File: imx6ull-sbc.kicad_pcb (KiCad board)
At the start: 4 copper layers, 210 parts, among them J1 Micro_SD_Card_Det1, J2 USB4105, J3 USB1130, J4 USB4105, J5 Barrel_Jack_Switch, J6 CRJ011-ML3-TH, Q1 SiSA35DN, SW1 CAS-220TA, U1 MX6UL-VM, U10 SFEM064GB1ED1TO-I-6F-111-STD, U11 TPD4EUSB30, U12 74LVC1G06, U13 D5V0H1B2LP, U14 D5V0H1B2LP, U15 TPS54233, U16 TPS2116DRLR, U17 INA219BxD, U18 DP83825IRMQR, U2 MC32PF1510A6EP, U3 MT41K256M16, U4 TUSB320, U5 AP22814AW5, U6 TPD4EUSB30, U7 D5V0H1B2LP, U8 D5V0H1B2LP, U9 W25Q32JVZP, Y1 24Mhz, Y2 32.768kHz

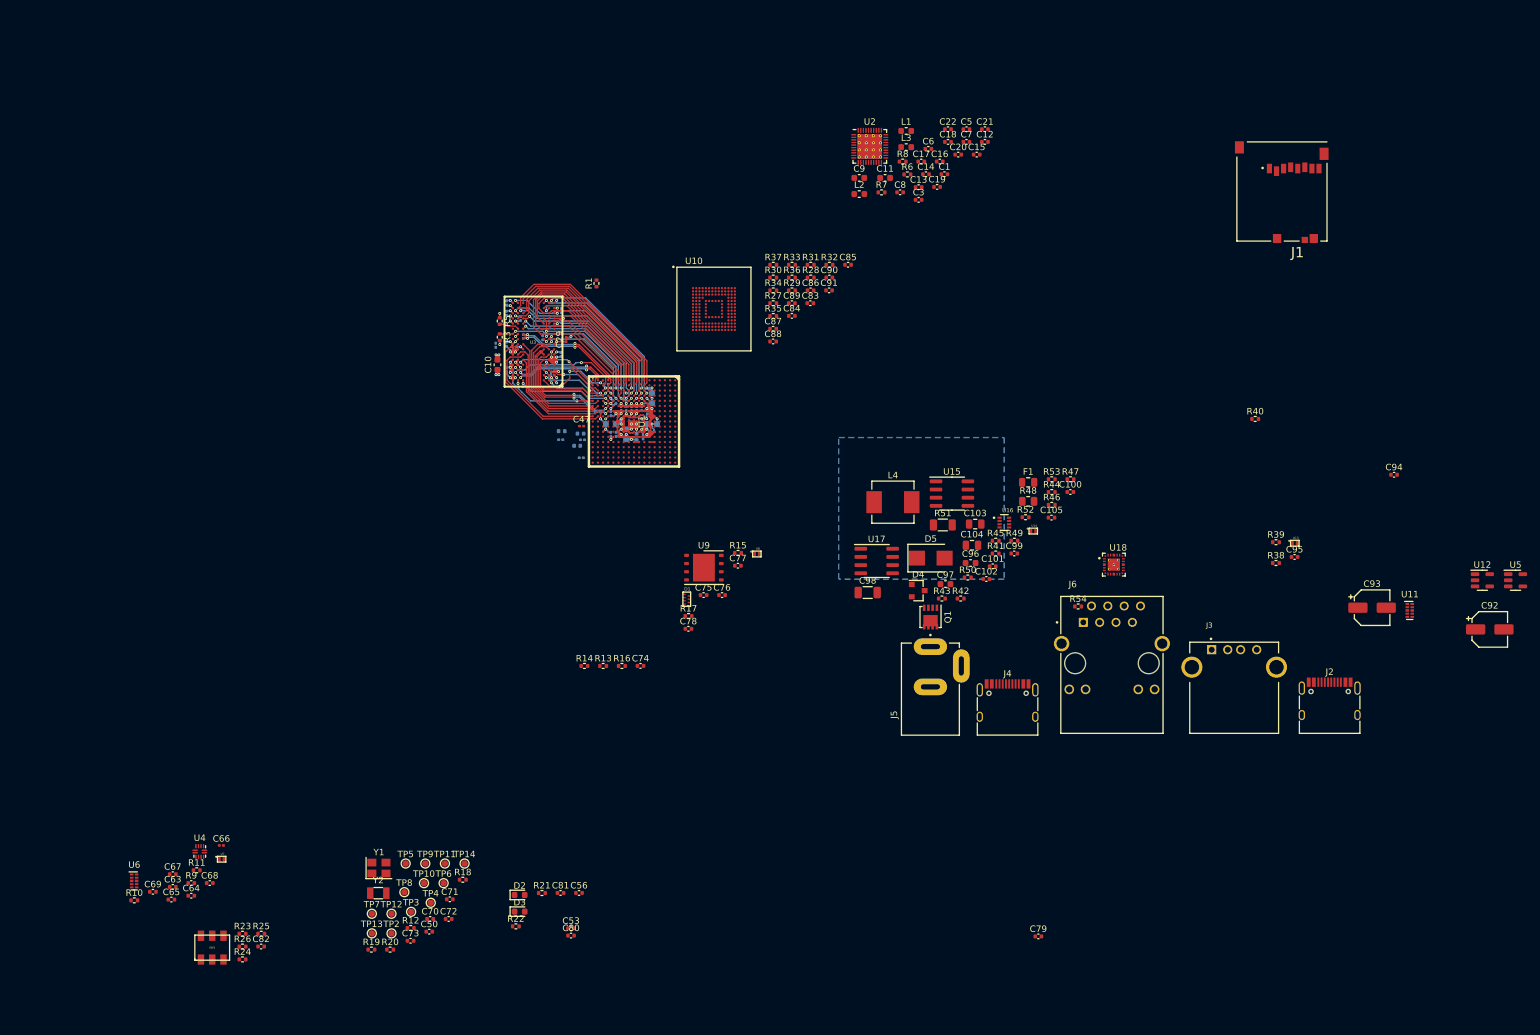
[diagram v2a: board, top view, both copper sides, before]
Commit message: move to hierarchal labels, work on power tree, add basic pcb layout
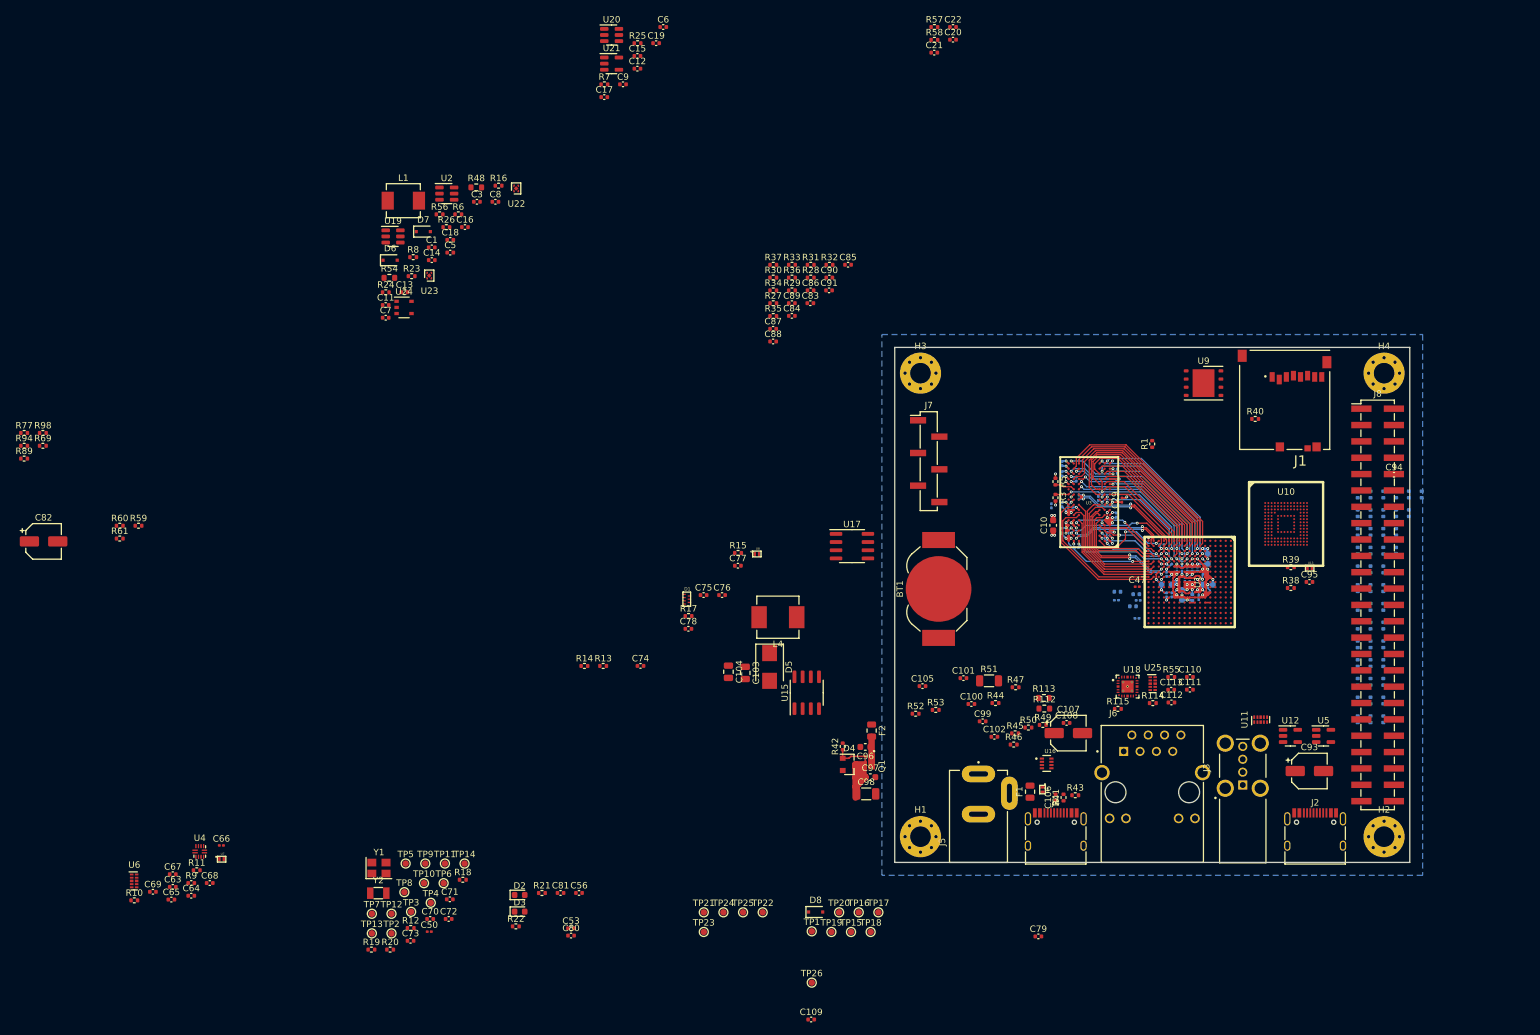
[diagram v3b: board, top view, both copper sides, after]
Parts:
- removed L2, L3: 1uH, Inductor_SMD:L_0603_1608Metric
- removed SW1: CAS-220TA, imx6ull-sbc:CAS-220-A
- added BT1: Battery_Cell, Battery:BatteryHolder_LINX_BAT-HLD-012-SMT, F.Cu at (151.8, 102.5)
- added C106: 0.1uF, Capacitor_SMD:C_0402_1005Metric, F.Cu at (170.0, 134.9)
- added C107: 120uF, Capacitor_SMD:CP_Elec_5x5.8, F.Cu at (172.0, 124.9)
- added C108: 0.1uF, Capacitor_SMD:C_0402_1005Metric, F.Cu at (171.7, 123.3)
- added C109: 18pF, Capacitor_SMD:C_0402_1005Metric, F.Cu at (132.0, 169.4)
- added C110: 10uF, Capacitor_SMD:C_0402_1005Metric, F.Cu at (190.8, 116.2)
- added C111: 10uF, Capacitor_SMD:C_0402_1005Metric, F.Cu at (190.8, 118.2)
- added C112: 1uF, Capacitor_SMD:C_0402_1005Metric, F.Cu at (188.0, 120.2)
- added C113: 1uF, Capacitor_SMD:C_0402_1005Metric, F.Cu at (187.9, 118.2)
- added D6: PMEG3010AESBYL, Diode_SMD:D_SOD-323F, F.Cu at (66.6, 51.5)
- added D7: PMEG3010AESBYL, Diode_SMD:D_SOD-323F, F.Cu at (71.8, 47.0)
- added D8: PMEG3010AESBYL, Diode_SMD:D_SOD-323F, F.Cu at (132.7, 152.7)
- added F2: Fuse, Fuse:Fuse_0805_2012Metric, F.Cu at (141.4, 124.5)
- added H1: MountingHole_Pad, MountingHole:MountingHole_3.2mm_M3_Pad_Via, F.Cu at (149.0, 141.0)
- added H2: MountingHole_Pad, MountingHole:MountingHole_3.2mm_M3_Pad_Via, F.Cu at (221.0, 141.0)
- added H3: MountingHole_Pad, MountingHole:MountingHole_3.2mm_M3_Pad_Via, F.Cu at (149.0, 69.0)
- added H4: MountingHole_Pad, MountingHole:MountingHole_3.2mm_M3_Pad_Via, F.Cu at (221.0, 69.0)
- added J7: Conn_01x06_Male, Connector_PinHeader_2.54mm:PinHeader_1x06_P2.54mm_Vertical_SMD_Pin1Left, F.Cu at (150.3, 82.7)
- added J8: Conn_02x25_Odd_Even, Connector_PinHeader_2.54mm:PinHeader_2x25_P2.54mm_Vertical_SMD, F.Cu at (220.0, 105.0)
- added R100: 10K, Resistor_SMD:R_0402_1005Metric, B.Cu at (218.9, 90.8)
- added R101: 10K, Resistor_SMD:R_0402_1005Metric, B.Cu at (224.9, 90.8)
- added R102: 10K, Resistor_SMD:R_0402_1005Metric, B.Cu at (216.9, 122.8)
- added R103: 10K, Resistor_SMD:R_0402_1005Metric, B.Cu at (218.9, 122.8)
- added R104: 10K, Resistor_SMD:R_0402_1005Metric, B.Cu at (226.9, 87.8)
- added R105: 10K, Resistor_SMD:R_0402_1005Metric, B.Cu at (218.9, 114.0)
- added R106: 10K, Resistor_SMD:R_0402_1005Metric, B.Cu at (216.9, 96.6)
- added R107: 10K, Resistor_SMD:R_0402_1005Metric, B.Cu at (220.9, 96.6)
- added R108: 10K, Resistor_SMD:R_0402_1005Metric, B.Cu at (216.9, 108.2)
- added R109: 10K, Resistor_SMD:R_0402_1005Metric, B.Cu at (218.9, 119.8)
- added R110: 1K, Resistor_SMD:R_0402_1005Metric, B.Cu at (224.9, 87.8)
- added R111: 1K, Resistor_SMD:R_0402_1005Metric, B.Cu at (218.9, 105.3)
- added R112: 0R, Resistor_SMD:R_0603_1608Metric, F.Cu at (168.2, 121.1)
- added R113: 0R, Resistor_SMD:R_0603_1608Metric, F.Cu at (168.2, 119.5)
- added R114: 2K2, Resistor_SMD:R_0402_1005Metric, F.Cu at (185.1, 120.2)
- added R115: 6.49K, Resistor_SMD:R_0402_1005Metric, F.Cu at (179.7, 121.2)
- added R55: 10R, Resistor_SMD:R_0402_1005Metric, F.Cu at (188.0, 116.2)
- added R56: 1K, Resistor_SMD:R_0402_1005Metric, F.Cu at (74.3, 44.3)
- added R57: 1.5K, Resistor_SMD:R_0402_1005Metric, F.Cu at (151.2, 15.2)
- added R58: 1.5K, Resistor_SMD:R_0402_1005Metric, F.Cu at (151.2, 17.2)
- added R59: 0R, Resistor_SMD:R_0402_1005Metric, F.Cu at (27.5, 92.7)
- added R60: 0R, Resistor_SMD:R_0402_1005Metric, F.Cu at (24.6, 92.7)
- added R61: 100K, Resistor_SMD:R_0402_1005Metric, F.Cu at (24.6, 94.7)
- added R62: 10K, Resistor_SMD:R_0402_1005Metric, B.Cu at (216.9, 111.1)
- added R63: 10K, Resistor_SMD:R_0402_1005Metric, B.Cu at (216.9, 99.5)
- added R64: 10K, Resistor_SMD:R_0402_1005Metric, B.Cu at (220.9, 111.1)
- added R65: 10K, Resistor_SMD:R_0402_1005Metric, B.Cu at (220.9, 114.0)
- added R66: 10K, Resistor_SMD:R_0402_1005Metric, B.Cu at (220.9, 99.5)
- added R67: 10K, Resistor_SMD:R_0402_1005Metric, B.Cu at (218.9, 96.6)
- added R68: 10K, Resistor_SMD:R_0402_1005Metric, B.Cu at (218.9, 102.4)
- added R69: 10K, Resistor_SMD:R_0402_1005Metric, F.Cu at (12.7, 80.3)
- added R70: 10K, Resistor_SMD:R_0402_1005Metric, B.Cu at (220.9, 90.8)
- added R71: 10K, Resistor_SMD:R_0402_1005Metric, B.Cu at (222.9, 87.8)
- added R72: 10K, Resistor_SMD:R_0402_1005Metric, B.Cu at (220.9, 87.8)
- added R73: 10K, Resistor_SMD:R_0402_1005Metric, B.Cu at (218.9, 116.9)
- added R74: 10K, Resistor_SMD:R_0402_1005Metric, B.Cu at (220.9, 122.8)
- added R75: 10K, Resistor_SMD:R_0402_1005Metric, B.Cu at (216.9, 90.8)
- added R76: 10K, Resistor_SMD:R_0402_1005Metric, B.Cu at (216.9, 119.8)
- added R77: 10K, Resistor_SMD:R_0402_1005Metric, F.Cu at (9.77, 78.3)
- added R78: 10K, Resistor_SMD:R_0402_1005Metric, B.Cu at (220.9, 93.7)
- added R79: 10K, Resistor_SMD:R_0402_1005Metric, B.Cu at (222.9, 90.8)
- added R80: 10K, Resistor_SMD:R_0402_1005Metric, B.Cu at (218.9, 111.1)
- added R81: 10K, Resistor_SMD:R_0402_1005Metric, B.Cu at (216.9, 116.9)
- added R82: 10K, Resistor_SMD:R_0402_1005Metric, B.Cu at (220.9, 108.2)
- added R83: 10K, Resistor_SMD:R_0402_1005Metric, B.Cu at (216.9, 93.7)
- added R84: 10K, Resistor_SMD:R_0402_1005Metric, B.Cu at (216.9, 102.4)
- added R85: 10K, Resistor_SMD:R_0402_1005Metric, B.Cu at (216.9, 114.0)
- added R86: 10K, Resistor_SMD:R_0402_1005Metric, B.Cu at (218.9, 99.5)
- added R87: 10K, Resistor_SMD:R_0402_1005Metric, B.Cu at (220.9, 105.3)
- added R88: 10K, Resistor_SMD:R_0402_1005Metric, B.Cu at (220.9, 102.4)
- added R89: 10K, Resistor_SMD:R_0402_1005Metric, F.Cu at (9.77, 82.3)
- added R90: 10K, Resistor_SMD:R_0402_1005Metric, B.Cu at (220.9, 119.8)
- added R91: 10K, Resistor_SMD:R_0402_1005Metric, B.Cu at (220.9, 116.9)
- added R92: 10K, Resistor_SMD:R_0402_1005Metric, B.Cu at (218.9, 87.8)
- added R93: 10K, Resistor_SMD:R_0402_1005Metric, B.Cu at (218.9, 108.2)
- added R94: 10K, Resistor_SMD:R_0402_1005Metric, F.Cu at (9.77, 80.3)
- added R95: 10K, Resistor_SMD:R_0402_1005Metric, B.Cu at (222.9, 93.7)
- added R96: 10K, Resistor_SMD:R_0402_1005Metric, B.Cu at (216.9, 105.3)
- added R97: 10K, Resistor_SMD:R_0402_1005Metric, B.Cu at (218.9, 93.7)
- added R98: 10K, Resistor_SMD:R_0402_1005Metric, F.Cu at (12.7, 78.3)
- added R99: 10K, Resistor_SMD:R_0402_1005Metric, B.Cu at (216.9, 87.8)
- added TP1: TestPoint, TestPoint:TestPoint_Pad_D1.0mm, F.Cu at (132.1, 155.7)
- added TP15: TestPoint, TestPoint:TestPoint_Pad_D1.0mm, F.Cu at (138.2, 155.8)
- added TP16: TestPoint, TestPoint:TestPoint_Pad_D1.0mm, F.Cu at (139.4, 152.8)
- added TP17: TestPoint, TestPoint:TestPoint_Pad_D1.0mm, F.Cu at (142.5, 152.8)
- added TP18: TestPoint, TestPoint:TestPoint_Pad_D1.0mm, F.Cu at (141.3, 155.8)
- added TP19: TestPoint, TestPoint:TestPoint_Pad_D1.0mm, F.Cu at (135.2, 155.8)
- added TP20: TestPoint, TestPoint:TestPoint_Pad_D1.0mm, F.Cu at (136.4, 152.8)
- added TP21: TestPoint, TestPoint:TestPoint_Pad_D1.0mm, F.Cu at (115.3, 152.8)
- added TP22: TestPoint, TestPoint:TestPoint_Pad_D1.0mm, F.Cu at (124.5, 152.8)
- added TP23: TestPoint, TestPoint:TestPoint_Pad_D1.0mm, F.Cu at (115.3, 155.8)
- added TP24: TestPoint, TestPoint:TestPoint_Pad_D1.0mm, F.Cu at (118.4, 152.8)
- added TP25: TestPoint, TestPoint:TestPoint_Pad_D1.0mm, F.Cu at (121.4, 152.8)
- added TP26: TestPoint, TestPoint:TestPoint_Pad_D1.0mm, F.Cu at (132.1, 163.7)
- added U19: TLV62569DDC, Package_TO_SOT_SMD:SOT-23-6, F.Cu at (67.1, 47.8)
- added U20: TLV62569DDC, Package_TO_SOT_SMD:SOT-23-6, F.Cu at (101.0, 16.5)
- added U21: TPS7A0333DBVR, Package_TO_SOT_SMD:SOT-23-5, F.Cu at (101.0, 20.9)
- added U22: NCP161BMX330TBG, imx6ull-sbc:XDFN4-1EP_1.0x1.0mm_EP0.52x0.52mm, F.Cu at (86.2, 40.3)
- added U23: NCP167AMX180TBG, imx6ull-sbc:XDFN4-1EP_1.0x1.0mm_EP0.52x0.52mm, F.Cu at (72.7, 53.8)
- added U24: NCP164CSNADJT1G, Package_SO:TSOP-5_1.65x3.05mm_P0.95mm, F.Cu at (68.8, 58.8)
- added U25: TPD4EUSB30, Package_SON:USON-10_2.5x1.0mm_P0.5mm, F.Cu at (185.1, 117.2)
- C11, C9: value 22uF -> 1uF; footprint Capacitor_SMD:C_0603_1608Metric -> Capacitor_SMD:C_0402_1005Metric
- C12, C14, C16, C18: value 10uF -> 1uF
- C13, C17: value 4.7uF -> 1uF
- C15, C22: value 10uF -> 0.1uF
- C19, C7, C8: value 1uF -> 10uF
- C20: value 10uF -> 4.7uF
- C21: value 0.47uF -> 0.1uF
- C3: value 0.1uF -> 0.22uF
- C5: value 0.1uF -> 4.7uF
- C50: footprint Capacitor_SMD:C_0402_1005Metric -> Capacitor_SMD:C_0201_0603Metric
- C6: value 2.2uF -> 10uF
- C82: value 0.22uF -> 120uF; footprint Capacitor_SMD:C_0402_1005Metric -> Capacitor_SMD:CP_Elec_5x5.8
- C92: value 120uF -> 0.22uF; footprint Capacitor_SMD:CP_Elec_5x5.8 -> Capacitor_SMD:C_0402_1005Metric; moved to B.Cu
- J3: value USB1130 -> USB-A-S-F-B-VU; footprint imx6ull-sbc:GCT_USB1130-15-A_REVA -> imx6ull-sbc:SAMTEC_USB-A-S-X-X-VU
- L1: value 1uH -> 2.2uH; footprint Inductor_SMD:L_0603_1608Metric -> Inductor_SMD:L_Vishay_IHLP-2020
- Q1: value SiSA35DN -> DMP4047LFDE-7; footprint Package_SO:Vishay_PowerPAK_1212-8_Single -> imx6ull-sbc:6-PowerUDFN
- R16: value 10R -> 100K
- R23: value 10K -> 0R
- R24: value 10K -> 499K
- R25: value 10K -> 442K
- R26: value 10K -> 100K
- R45: value 0R -> 3.3K
- R46: value 0R -> 1K
- R48: footprint Resistor_SMD:R_0805_2012Metric -> Resistor_SMD:R_0603_1608Metric
- R54: value 10K -> 0R; footprint Resistor_SMD:R_0402_1005Metric -> Resistor_SMD:R_0603_1608Metric
- R6: value 100K -> 10K
- R7: value 100K -> 1M
- U10: footprint imx6ull-sbc:BGA153N50P14X14_1150X1300X100 -> imx6ull-sbc:FBGA-153
- U18: value DP83825IRMQR -> DP83825
- U2: value MC32PF1510A6EP -> TLV62569DDC; footprint Package_DFN_QFN:QFN-40-1EP_5x5mm_P0.4mm_EP3.8x3.8mm_ThermalVias -> Package_TO_SOT_SMD:SOT-23-6
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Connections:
- C1 pad 1: DDR_1V35 -> ~{WDOG}
- C1 pad 2: GND -> Net-(C1-Pad2)
- C103 pad 1: Net-(C103-Pad1) -> /VIN/JACK_5V_VIN
- C104 pad 1: Net-(C103-Pad1) -> /VIN/JACK_5V_VIN
- C105 pad 1: /VIN/DCDC_3V3 -> DCDC_3V3
- C11 pad 1: /PMIC/VSYS -> VSYS_5V
- C12 pad 1: VDD_ARM_SOC_IN -> VSYS_5V
- C13 pad 1: EMMC_1V8 -> Net-(C13-Pad1)
- C14 pad 1: VDD_ARM_SOC_IN -> /Power/VDD_SNVS_3V3
- C15 pad 1: LDO2_3V3 -> Net-(BT1-Pad1)
- C16 pad 1: DDR_1V35 -> LDO_3V3
- C17 pad 1: SD_3V3_1V8 -> Net-(C17-Pad1)
- C18 pad 1: DDR_1V35 -> Net-(C18-Pad1)
- C19 pad 1: DDR_VREF -> Net-(BT1-Pad1)
- C20 pad 1: DCDC_3V3 -> DDR_1V35
- C20 pad 2: GND -> Net-(C20-Pad2)
- C21 pad 1: /PMIC/VSNVS_3V -> DDR_1V35
- C21 pad 2: GND -> /DDR/VREFDDR
- C22 pad 1: DCDC_3V3 -> /DDR/VREFDDR
- C22 pad 2: GND -> Net-(C20-Pad2)
- C24 pad 1: DDR_VREF -> /DDR/VREFDDR
- C28 pad 1: DDR_VREF -> /DDR/VREFDDR
- C29 pad 1: DDR_VREF -> /DDR/VREFDDR
- C3 pad 1: DCDC_3V3 -> Net-(C3-Pad1)
- C42 pad 1: LDO2_3V3 -> DCDC_3V3
- C44 pad 1: LDO2_3V3 -> DCDC_3V3
- C47 pad 1: LDO2_3V3 -> SNVS_3V3
- C5 pad 1: /PMIC/LICELL -> VSYS_5V
- C53 pad 1: LDO2_3V3 -> LDO_3V3
- C56 pad 1: LDO2_3V3 -> LDO_3V3
- C6 pad 1: VSYS_5V -> Net-(C6-Pad1)
- C7 pad 1: /PMIC/VCORE -> Net-(C6-Pad1)
- C74 pad 1: EMMC_1V8 -> LDO_1V8
- C8 pad 1: /PMIC/VDIG -> Net-(C6-Pad1)
- C82 pad 1: DCDC_3V3 -> /USB/VBUS_1
- C85 pad 1: EMMC_1V8 -> LDO_1V8
- C87 pad 1: EMMC_1V8 -> LDO_1V8
- C89 pad 1: EMMC_1V8 -> LDO_1V8
- C9 pad 1: /PMIC/VSYS -> VSYS_5V
- C91 pad 1: EMMC_1V8 -> LDO_1V8
- C92 pad 1: /USB/VBUS_1 -> DCDC_3V3
- D2 pad 1: unconnected-(D2-Pad1) -> Net-(U1-PadE4)
- D2 pad 2: unconnected-(D2-Pad2) -> Net-(D2-Pad2)
- D3 pad 1: unconnected-(D3-Pad1) -> Net-(U1-PadE3)
- D3 pad 2: unconnected-(D3-Pad2) -> Net-(D3-Pad2)
- J3 pad 2: /USB/USB2D_P -> /USB/USB2D_N
- J3 pad 3: /USB/USB2D_N -> /USB/USB2D_P
- J5 pad 1: Net-(C96-Pad1) -> Net-(J5-Pad1)
- L1 pad 2: VDD_ARM_SOC_IN -> Net-(C6-Pad1)
- L4 pad 2: Net-(C103-Pad1) -> /VIN/JACK_5V_VIN
- R11 pad 2: USB1_INT_B -> ~{USB1_INT}
- R16 pad 1: /Storage/QSPI_nCS -> Net-(C3-Pad1)
- R16 pad 2: Net-(R16-Pad2) -> GND
- R17 pad 2: Net-(R16-Pad2) -> /Storage/QSPI_nCS
- R18 pad 1: LDO2_3V3 -> SNVS_3V3
- R19 pad 1: LDO2_3V3 -> SNVS_3V3
- R21 pad 2: I2C1_SCL -> I2C1_SDA
- R22 pad 2: I2C1_SDA -> I2C1_SCL
- R23 pad 1: /Boot Configuration/BT_CFG1[6] -> Net-(D6-Pad2)
- R23 pad 2: Net-(R23-Pad2) -> Net-(C3-Pad1)
- R24 pad 1: /Boot Configuration/BT_CFG1[4] -> VSYS_5V
- R24 pad 2: Net-(R24-Pad2) -> /Power/PG_3V3
- R25 pad 1: DCDC_3V3 -> Net-(C6-Pad1)
- R25 pad 2: /Boot Configuration/BT_CFG1[4] -> Net-(R25-Pad2)
- R26 pad 1: /Boot Configuration/BT_CFG2[1] -> Net-(R25-Pad2)
- R26 pad 2: Net-(R23-Pad2) -> GND
- R28 pad 1: EMMC_1V8 -> LDO_1V8
- R29 pad 1: EMMC_1V8 -> LDO_1V8
- R30 pad 1: EMMC_1V8 -> LDO_1V8
- R31 pad 1: EMMC_1V8 -> LDO_1V8
- R32 pad 1: EMMC_1V8 -> LDO_1V8
- R33 pad 1: EMMC_1V8 -> LDO_1V8
- R34 pad 1: EMMC_1V8 -> LDO_1V8
- R35 pad 1: EMMC_1V8 -> LDO_1V8
- R36 pad 1: EMMC_1V8 -> LDO_1V8
- R36 pad 2: /Storage/SD2_CMD -> /Storage/SD2_nRST
- R37 pad 1: EMMC_1V8 -> LDO_1V8
- R37 pad 2: /Storage/SD2_nRST -> /Storage/SD2_CMD
- R45 pad 2: Net-(R45-Pad2) -> Net-(U16-Pad4)
- R46 pad 1: Net-(R45-Pad2) -> Net-(U16-Pad4)
- R47 pad 1: /VIN/DCDC_3V3 -> DCDC_3V3
- R47 pad 2: /VIN/ATS_STATUS -> ATS_STATUS
- R48 pad 1: Net-(C103-Pad1) -> Net-(C6-Pad1)
- R48 pad 2: Net-(R48-Pad2) -> DCDC_3V3
- R49 pad 1: Net-(C103-Pad1) -> /VIN/JACK_5V_VIN
- R51 pad 2: /VIN/VSYS_5V -> VSYS_5V
- R54 pad 1: /VIN/DCDC_3V3 -> Net-(C17-Pad1)
- R54 pad 2: /VIN/ATS_SELECT -> LDO_1V8
- R6 pad 1: /PMIC/VSNVS_3V -> /Power/PMIC_ON_REQ
- R6 pad 2: PMIC_WDI -> Net-(C3-Pad1)
- R7 pad 1: Net-(R7-Pad1) -> Net-(C1-Pad2)
- R7 pad 2: /PMIC/VSNVS_3V -> GND
- R8 pad 1: Net-(R8-Pad1) -> VSYS_5V
- R8 pad 2: /PMIC/VSYS -> Net-(C3-Pad1)
- U1 pad A10: /Boot Configuration/BT_CFG1[6] -> /Peripherals/BT_CFG1[6]
- U1 pad A11: /Boot Configuration/BT_CFG2[1] -> /Peripherals/BT_CFG2[1]
- U1 pad A12: /Boot Configuration/BT_CFG2[6] -> /Peripherals/BT_CFG2[6]
- U1 pad A13: /Boot Configuration/BT_CFG4[2] -> /Peripherals/BT_CFG4[2]
- U1 pad A14: /Boot Configuration/BT_CFG4[6] -> /Peripherals/BT_CFG4[6]
- U1 pad A8: unconnected-(U1-PadA8) -> /Peripherals/GPIO3_IO00
- U1 pad A9: /Boot Configuration/BT_CFG1[1] -> /Peripherals/BT_CFG1[1]
- U1 pad B10: /Boot Configuration/BT_CFG1[5] -> /Peripherals/BT_CFG1[5]
- U1 pad B11: /Boot Configuration/BT_CFG2[0] -> /Peripherals/BT_CFG2[0]
- U1 pad B12: /Boot Configuration/BT_CFG1[6] -> /Peripherals/BT_CFG2[5]
- U1 pad B13: /Boot Configuration/BT_CFG4[1] -> /Peripherals/BT_CFG4[1]
- U1 pad B14: /Boot Configuration/BT_CFG4[5] -> /Peripherals/BT_CFG4[5]
- U1 pad B16: /Boot Configuration/BT_CFG4[7] -> /Peripherals/BT_CFG4[7]
- U1 pad B8: unconnected-(U1-PadB8) -> /Peripherals/GPIO3_IO01
- U1 pad B9: /Boot Configuration/BT_CFG1[0] -> /Peripherals/BT_CFG1[0]
- U1 pad C10: /Boot Configuration/BT_CFG1[4] -> /Peripherals/BT_CFG1[4]
- U1 pad C12: /Boot Configuration/BT_CFG2[4] -> /Peripherals/BT_CFG2[4]
- U1 pad C13: /Boot Configuration/BT_CFG4[0] -> /Peripherals/BT_CFG4[0]
- U1 pad C14: /Boot Configuration/BT_CFG4[4] -> /Peripherals/BT_CFG4[4]
- U1 pad C16: unconnected-(U1-PadC16) -> /Ethernet/ENET1_MDC
- U1 pad C17: unconnected-(U1-PadC17) -> /Ethernet/ENET1_MDIO
- U1 pad C9: unconnected-(U1-PadC9) -> /Peripherals/GPIO3_IO03
- U1 pad D1: unconnected-(U1-PadD1) -> SD1_VSELECT
- U1 pad D10: /Boot Configuration/BT_CFG1[3] -> /Peripherals/BT_CFG1[3]
- U1 pad D11: /Boot Configuration/BT_CFG1[7] -> /Peripherals/BT_CFG1[7]
- U1 pad D12: /Boot Configuration/BT_CFG2[3] -> /Peripherals/BT_CFG2[3]
- U1 pad D13: /Boot Configuration/BT_CFG2[7] -> /Peripherals/BT_CFG2[7]
- U1 pad D14: /Boot Configuration/BT_CFG4[3] -> /Peripherals/BT_CFG4[3]
- U1 pad D15: unconnected-(U1-PadD15) -> /Ethernet/ENET1_RX_ER
- U1 pad D17: unconnected-(U1-PadD17) -> /Ethernet/~{ENET1_RST}
- U1 pad D2: unconnected-(U1-PadD2) -> /Peripherals/GPIO4_IO27
- U1 pad D3: unconnected-(U1-PadD3) -> /Peripherals/GPIO4_IO26
- U1 pad D4: unconnected-(U1-PadD4) -> /Peripherals/GPIO4_IO25
- U1 pad D9: unconnected-(U1-PadD9) -> /Peripherals/GPIO3_IO02
- U1 pad E1: unconnected-(U1-PadE1) -> /Peripherals/GPIO4_IO24
- U1 pad E10: /Boot Configuration/BT_CFG1[2] -> /Peripherals/BT_CFG1[2]
- U1 pad E12: /Boot Configuration/BT_CFG2[2] -> /Peripherals/BT_CFG2[2]
- U1 pad E14: unconnected-(U1-PadE14) -> /Ethernet/ENET1_TX_DATA1
- U1 pad E15: unconnected-(U1-PadE15) -> /Ethernet/ENET1_TX_DATA0
- U1 pad E16: unconnected-(U1-PadE16) -> /Ethernet/ENET1_CRS_DV
- U1 pad E17: unconnected-(U1-PadE17) -> /Ethernet/ENET1_RX_DATA1
- U1 pad E2: unconnected-(U1-PadE2) -> /Peripherals/GPIO4_IO23
- U1 pad E3: unconnected-(U1-PadE3) -> Net-(U1-PadE3)
- U1 pad E4: unconnected-(U1-PadE4) -> Net-(U1-PadE4)
- U1 pad E5: unconnected-(U1-PadE5) -> I2C1_SCL
- U1 pad E7: EMMC_1V8 -> LDO_1V8
- U1 pad E9: unconnected-(U1-PadE9) -> ~{WDOG}
- U1 pad F14: unconnected-(U1-PadF14) -> /Ethernet/ENET1_TX_CLK_R
- U1 pad F15: unconnected-(U1-PadF15) -> /Ethernet/ENET1_TX_EN
- U1 pad F16: unconnected-(U1-PadF16) -> /Ethernet/ENET1_RX_DATA0
- U1 pad F2: unconnected-(U1-PadF2) -> ~{USB1_INT}
- U1 pad F5: unconnected-(U1-PadF5) -> I2C1_SDA
- U1 pad K13: USB1_INT_B -> USB1_ID
- U1 pad K17: unconnected-(U1-PadK17) -> /Peripherals/GPIO1_IO06
- U1 pad L13: LDO2_3V3 -> LDO_3V3
- U1 pad L14: I2C1_SCL -> /Peripherals/GPIO1_IO02
- U1 pad L15: unconnected-(U1-PadL15) -> /Peripherals/GPIO1_IO01
- U1 pad L16: unconnected-(U1-PadL16) -> /Peripherals/GPIO1_IO07
- U1 pad L17: I2C1_SDA -> /Peripherals/GPIO1_IO03
- U1 pad M13: LDO2_3V3 -> LDO_3V3
- U1 pad M15: PMIC_WDI -> /Peripherals/GPIO1_IO09
- U1 pad M16: unconnected-(U1-PadM16) -> /Peripherals/GPIO1_IO04
- U1 pad M17: unconnected-(U1-PadM17) -> /Peripherals/GPIO1_IO05
- U1 pad N13: LDO2_3V3 -> DCDC_3V3
- U1 pad N17: unconnected-(U1-PadN17) -> /Peripherals/GPIO1_IO08
- U1 pad P12: LDO2_3V3 -> SNVS_3V3
- U1 pad P4: DDR_VREF -> /DDR/VREFDDR
- U1 pad R10: unconnected-(U1-PadR10) -> /Control/GPIO_DVFS
- U1 pad R8: unconnected-(U1-PadR8) -> /Control/ONOFF
- U1 pad R9: unconnected-(U1-PadR9) -> ATS_STATUS
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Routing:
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- added copper zone on In1.Cu, net GND
- removed copper zone on In1.Cu, net DCDC_3V3
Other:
- board outline added: 80 x 80 mm

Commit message: most of sch done, inital component pcb placement
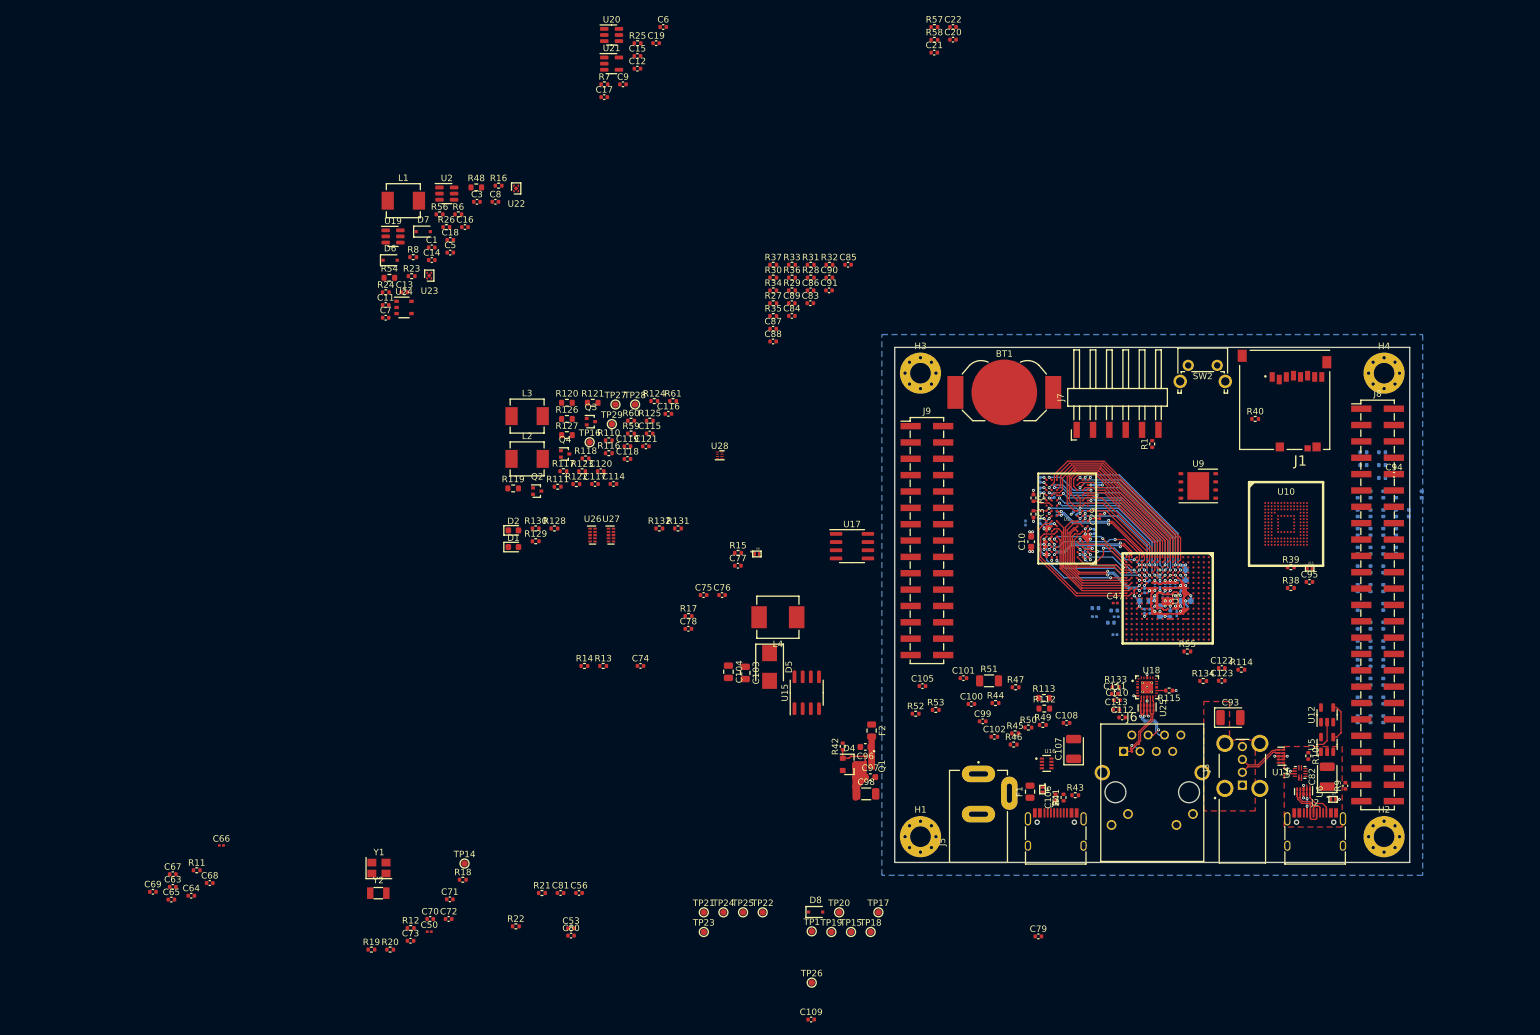
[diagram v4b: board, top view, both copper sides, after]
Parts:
- removed D3: LED, LED_SMD:LED_0603_1608Metric
- removed TP10, TP11, TP12, TP13, TP2, TP3, TP4, TP5, TP6, TP7, TP8, TP9: TestPoint, TestPoint:TestPoint_Pad_D1.0mm
- added C114: 4.7uF, Capacitor_SMD:C_0402_1005Metric, F.Cu at (101.3, 86.2)
- added C115: 4.7uF, Capacitor_SMD:C_0402_1005Metric, F.Cu at (106.9, 78.4)
- added C116: 10uF, Capacitor_SMD:C_0402_1005Metric, F.Cu at (109.8, 75.3)
- added C117: 10uF, Capacitor_SMD:C_0402_1005Metric, F.Cu at (98.4, 86.2)
- added C118: 10uF, Capacitor_SMD:C_0402_1005Metric, F.Cu at (103.5, 82.3)
- added C119: 10uF, Capacitor_SMD:C_0402_1005Metric, F.Cu at (103.5, 80.4)
- added C120: 10uF, Capacitor_SMD:C_0402_1005Metric, F.Cu at (99.3, 84.2)
- added C121: 10uF, Capacitor_SMD:C_0402_1005Metric, F.Cu at (106.3, 80.4)
- added C122: 0.1uF, Capacitor_SMD:C_0402_1005Metric, F.Cu at (195.8, 114.8)
- added C123: 0.1uF, Capacitor_SMD:C_0402_1005Metric, F.Cu at (195.8, 116.8)
- added J9: Conn_02x15_Odd_Even, Connector_PinHeader_2.54mm:PinHeader_2x15_P2.54mm_Vertical_SMD, F.Cu at (150.0, 95.0)
- added L2: 2.2uH, Inductor_SMD:L_Vishay_IHLP-2020, F.Cu at (87.9, 82.3)
- added L3: 2.2uH, Inductor_SMD:L_Vishay_IHLP-2020, F.Cu at (87.9, 75.7)
- added Q2: 2SK3019, Package_TO_SOT_SMD:SOT-416, F.Cu at (89.5, 87.3)
- added Q3: 2SK3019, Package_TO_SOT_SMD:SOT-416, F.Cu at (97.8, 76.5)
- added Q4: 2SK3019, Package_TO_SOT_SMD:SOT-416, F.Cu at (93.8, 81.5)
- added R116: 953K, Resistor_SMD:R_0402_1005Metric, F.Cu at (100.6, 81.4)
- added R117: 100K, Resistor_SMD:R_0402_1005Metric, F.Cu at (93.5, 84.2)
- added R118: 91K, Resistor_SMD:R_0402_1005Metric, F.Cu at (97.0, 82.2)
- added R119: 0R, Resistor_SMD:R_0603_1608Metric, F.Cu at (85.7, 86.9)
- added R120: 0R, Resistor_SMD:R_0603_1608Metric, F.Cu at (94.1, 73.6)
- added R121: 0R, Resistor_SMD:R_0603_1608Metric, F.Cu at (98.1, 73.6)
- added R122: 200K, Resistor_SMD:R_0402_1005Metric, F.Cu at (95.5, 86.2)
- added R123: 100K, Resistor_SMD:R_0402_1005Metric, F.Cu at (96.4, 84.2)
- added R124: 100K, Resistor_SMD:R_0402_1005Metric, F.Cu at (107.7, 73.3)
- added R125: 93.1K, Resistor_SMD:R_0402_1005Metric, F.Cu at (107.0, 76.4)
- added R126: 0R, Resistor_SMD:R_0603_1608Metric, F.Cu at (94.1, 76.1)
- added R127: 0R, Resistor_SMD:R_0603_1608Metric, F.Cu at (94.1, 78.6)
- added R128: 1K, Resistor_SMD:R_0402_1005Metric, F.Cu at (92.1, 93.1)
- added R129: 1K, Resistor_SMD:R_0402_1005Metric, F.Cu at (89.2, 95.1)
- added R130: 0R, Resistor_SMD:R_0402_1005Metric, F.Cu at (89.2, 93.1)
- added R131: 2.49K, Resistor_SMD:R_0402_1005Metric, F.Cu at (111.3, 93.1)
- added R132: 2.49K, Resistor_SMD:R_0402_1005Metric, F.Cu at (108.4, 93.1)
- added R133: 1K, Resistor_SMD:R_0402_1005Metric, F.Cu at (179.3, 117.8)
- added R134: 1K, Resistor_SMD:R_0402_1005Metric, F.Cu at (192.9, 116.8)
- added SW2: SW_Push, Button_Switch_THT:SW_Tactile_SPST_Angled_PTS645Vx58-2LFS, F.Cu at (190.6, 67.8)
- added TP27: TestPoint, TestPoint:TestPoint_Pad_D1.0mm, F.Cu at (101.6, 73.9)
- added TP28: TestPoint, TestPoint:TestPoint_Pad_D1.0mm, F.Cu at (104.7, 73.9)
- added TP29: TestPoint, TestPoint:TestPoint_Pad_D1.0mm, F.Cu at (101.1, 76.9)
- added U26: TPD4EUSB30, Package_SON:USON-10_2.5x1.0mm_P0.5mm, F.Cu at (98.1, 94.2)
- added U27: TPD4EUSB30, Package_SON:USON-10_2.5x1.0mm_P0.5mm, F.Cu at (100.9, 94.2)
- added U28: 74LVC1G123, imx6ull-sbc:SOT1203, F.Cu at (117.8, 81.8)
- C107, C82, C93: value 120uF -> 100uF; footprint Capacitor_SMD:CP_Elec_5x5.8 -> Capacitor_Tantalum_SMD:CP_EIA-3528-15_AVX-H
- D1: value PUSB3TB6 -> LED; footprint imx6ull-sbc:SOT1358-1 -> LED_SMD:LED_0603_1608Metric
- J6: value CRJ011-ML3-TH -> J1B1211CCD; footprint imx6ull-sbc:CUI_CRJ011-ML3-TH -> imx6ull-sbc:J1B1211CCD
- J7: footprint Connector_PinHeader_2.54mm:PinHeader_1x06_P2.54mm_Vertical_SMD_Pin1Left -> Connector_Harwin:Harwin_M20-89006xx_1x06_P2.54mm_Horizontal
- R110, R111: value 1K -> 100K; moved to F.Cu
- R114: value 2K2 -> 2.2K
- R59: value 0R -> 124K
- R60: value 0R -> 100K
- R61: value 100K -> 133K
- R69, R77, R89, R94, R98: moved to B.Cu
- U12: value 74LVC1G06 -> 74LVC1G04
- moved R77 211.0 mm to (220.7, 81.3), turned to 180 degrees
- moved R89 211.0 mm to (220.7, 85.3), turned to 180 degrees
- moved R94 211.0 mm to (220.7, 83.3), turned to 180 degrees
- moved R69 205.1 mm to (217.8, 83.3), turned to 180 degrees
- moved R98 205.1 mm to (217.8, 81.3), turned to 180 degrees
- moved C82 202.7 mm to (212.2, 131.7), turned to 90 degrees
- moved R10 183.7 mm to (209.2, 128.4), turned to -90 degrees
- moved U6 182.2 mm to (208.5, 134.0), turned to -90 degrees
- moved R9 179.9 mm to (215.0, 133.1), turned to 90 degrees
- moved U7 172.9 mm to (213.1, 135.2)
- moved U4 171.4 mm to (208.0, 131.0), turned to 90 degrees
- moved R111 127.6 mm to (92.6, 86.6), turned to 0 degrees
- moved R110 124.6 mm to (100.6, 79.4), turned to 0 degrees
- moved R61 88.6 mm to (110.6, 73.3)
- moved TP16 84.1 mm to (97.6, 79.7)
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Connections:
- net /Control/PMIC_STBY_REQ renamed PMIC_STBY_REQ
- C16 pad 1: LDO_3V3 -> /Power/LDO_3V3_R
- C17 pad 1: Net-(C17-Pad1) -> /Power/LDO_1V8_R
- C18 pad 1: Net-(C18-Pad1) -> /Power/SD_3V3_1V8_R
- C6 pad 1: Net-(C6-Pad1) -> /Power/DCDC_3V3_R
- C7 pad 1: Net-(C6-Pad1) -> /Power/DCDC_3V3_R
- C8 pad 1: Net-(C6-Pad1) -> /Power/DCDC_3V3_R
- D1 pad 1: /Storage/SD1_DATA1 -> /Peripherals/LED_0
- D1 pad 2: /Storage/SD1_CLK -> Net-(D1-Pad2)
- D2 pad 1: Net-(U1-PadE4) -> /Peripherals/LED_1
- D7 pad 1: SNVS_3V3 -> Net-(D7-Pad1)
- D8 pad 1: SNVS_3V3 -> Net-(D7-Pad1)
- J6 pad 10: unconnected-(J6-Pad10) -> /Ethernet/RJ45_LED_G
- J6 pad 11: unconnected-(J6-Pad11) -> GND
- J6 pad 12: unconnected-(J6-Pad12) -> /Ethernet/RJ45_LED_Y
- J6 pad 9: unconnected-(J6-Pad9) -> GND
- J7 pad 1: unconnected-(J7-Pad1) -> GND
- J7 pad 2: /Control/UART1_TX -> /Control/UART1_RTS
- J7 pad 3: /Control/UART1_RX -> unconnected-(J7-Pad3)
- J7 pad 4: unconnected-(J7-Pad4) -> /Control/UART1_RX
- J7 pad 5: /Control/UART1_RTS -> /Control/UART1_TX
- J7 pad 6: GND -> unconnected-(J7-Pad6)
- J8 pad 1: GND -> VSYS_5V
- J8 pad 10: /Peripherals/GPIO1_IO03 -> /Peripherals/BT_CFG4[1]
- J8 pad 11: /Peripherals/BT_CFG1[4] -> /Peripherals/BT_CFG1[2]
- J8 pad 12: /Peripherals/GPIO1_IO04 -> /Peripherals/BT_CFG4[2]
- J8 pad 13: /Peripherals/BT_CFG1[5] -> /Peripherals/BT_CFG1[3]
- J8 pad 14: /Peripherals/GPIO1_IO05 -> /Peripherals/BT_CFG4[3]
- J8 pad 15: /Peripherals/BT_CFG1[6] -> /Peripherals/BT_CFG1[4]
- J8 pad 16: /Peripherals/GPIO1_IO06 -> /Peripherals/BT_CFG4[4]
- J8 pad 17: /Peripherals/BT_CFG1[7] -> /Peripherals/BT_CFG1[5]
- J8 pad 18: /Peripherals/GPIO1_IO07 -> /Peripherals/BT_CFG4[5]
- J8 pad 19: /Peripherals/BT_CFG2[0] -> /Peripherals/BT_CFG1[6]
- J8 pad 2: GND -> DCDC_3V3
- J8 pad 20: /Peripherals/GPIO1_IO08 -> /Peripherals/BT_CFG4[6]
- J8 pad 21: /Peripherals/BT_CFG2[1] -> /Peripherals/BT_CFG1[7]
- J8 pad 22: /Peripherals/GPIO1_IO09 -> /Peripherals/BT_CFG4[7]
- J8 pad 23: /Peripherals/BT_CFG2[2] -> GND
- J8 pad 25: /Peripherals/BT_CFG2[3] -> /Peripherals/BT_CFG2[0]
- J8 pad 26: /Peripherals/GPIO3_IO00 -> /Peripherals/GPIO1_IO01
- J8 pad 27: /Peripherals/BT_CFG2[4] -> /Peripherals/BT_CFG2[1]
- J8 pad 28: /Peripherals/GPIO3_IO01 -> /Peripherals/GPIO1_IO02
- J8 pad 29: /Peripherals/BT_CFG2[5] -> /Peripherals/BT_CFG2[2]
- J8 pad 3: /Peripherals/BT_CFG1[0] -> VSYS_5V
- J8 pad 30: /Peripherals/GPIO3_IO02 -> /Peripherals/GPIO1_IO03
- J8 pad 31: /Peripherals/BT_CFG2[6] -> /Peripherals/BT_CFG2[3]
- J8 pad 32: /Peripherals/GPIO3_IO03 -> /Peripherals/GPIO1_IO04
- J8 pad 33: /Peripherals/BT_CFG2[7] -> /Peripherals/BT_CFG2[4]
- J8 pad 34: GND -> /Peripherals/GPIO1_IO05
- J8 pad 35: /Peripherals/BT_CFG4[0] -> /Peripherals/BT_CFG2[5]
- J8 pad 36: /Peripherals/GPIO4_IO23 -> /Peripherals/GPIO1_IO06
- J8 pad 37: /Peripherals/BT_CFG4[1] -> /Peripherals/BT_CFG2[6]
- J8 pad 38: /Peripherals/GPIO4_IO24 -> /Peripherals/GPIO1_IO07
- J8 pad 39: /Peripherals/BT_CFG4[2] -> /Peripherals/BT_CFG2[7]
- J8 pad 4: unconnected-(J8-Pad4) -> DCDC_3V3
- J8 pad 40: /Peripherals/GPIO4_IO25 -> /Peripherals/GPIO1_IO08
- J8 pad 41: /Peripherals/BT_CFG4[3] -> /Peripherals/GPIO4_IO24
- J8 pad 42: /Peripherals/GPIO4_IO26 -> /Peripherals/GPIO1_IO09
- J8 pad 43: /Peripherals/BT_CFG4[4] -> /Peripherals/GPIO4_IO23
- J8 pad 44: /Peripherals/GPIO4_IO27 -> /Peripherals/GPIO4_IO25
- J8 pad 45: /Peripherals/BT_CFG4[5] -> /Peripherals/GPIO4_IO22
- J8 pad 46: GND -> /Peripherals/GPIO4_IO26
- J8 pad 47: /Peripherals/BT_CFG4[6] -> /Peripherals/GPIO4_IO21
- J8 pad 48: DCDC_3V3 -> /Peripherals/GPIO4_IO27
- J8 pad 49: /Peripherals/BT_CFG4[7] -> GND
- J8 pad 5: /Peripherals/BT_CFG1[1] -> GND
- J8 pad 50: DCDC_3V3 -> GND
- J8 pad 6: /Peripherals/GPIO1_IO01 -> GND
- J8 pad 7: /Peripherals/BT_CFG1[2] -> /Peripherals/BT_CFG1[0]
- J8 pad 8: /Peripherals/GPIO1_IO02 -> /Peripherals/BT_CFG4[0]
- J8 pad 9: /Peripherals/BT_CFG1[3] -> /Peripherals/BT_CFG1[1]
- L1 pad 2: Net-(C6-Pad1) -> /Power/DCDC_3V3_R
- R110 pad 1: DCDC_3V3 -> Net-(U2-Pad6)
- R110 pad 2: Net-(D2-Pad2) -> GND
- R111 pad 1: DCDC_3V3 -> GPIO_DVFS
- R111 pad 2: Net-(D3-Pad2) -> GND
- R18 pad 2: Net-(R18-Pad2) -> /Control/BOOT_MODE0
- R19 pad 2: Net-(R19-Pad2) -> /Control/BOOT_MODE1
- R25 pad 1: Net-(C6-Pad1) -> /Power/DCDC_3V3_R
- R48 pad 1: Net-(C6-Pad1) -> /Power/DCDC_3V3_R
- R54 pad 1: Net-(C17-Pad1) -> /Power/LDO_1V8_R
- R56 pad 1: SNVS_3V3 -> Net-(D7-Pad1)
- R59 pad 1: Net-(R18-Pad2) -> /Power/DDR_1V35_R
- R59 pad 2: Net-(U1-PadU10) -> Net-(U20-Pad6)
- R6 pad 1: /Power/PMIC_ON_REQ -> PMIC_ON_REQ
- R60 pad 1: Net-(R19-Pad2) -> Net-(U20-Pad6)
- R60 pad 2: Net-(U1-PadT10) -> GND
- R61 pad 1: SNVS_3V3 -> /Power/VDD_ARM_SOC_IN_R
- R61 pad 2: /Control/JTAG_nSRST -> Net-(U2-Pad6)
- TP15 pad 1: unconnected-(TP15-Pad1) -> /Power/DDR_1V35_R
- TP16 pad 1: unconnected-(TP16-Pad1) -> /Power/DDR_PG
- TP17 pad 1: DCDC_3V3 -> /Power/DCDC_3V3_R
- TP18 pad 1: unconnected-(TP18-Pad1) -> /Power/SD_3V3_1V8_R
- TP19 pad 1: LDO_1V8 -> /Power/LDO_1V8_R
- TP20 pad 1: SNVS_3V3 -> Net-(D7-Pad1)
- TP21 pad 1: Net-(U1-PadT10) -> /Control/BOOT_MODE0
- TP22 pad 1: Net-(U1-PadU10) -> /Control/BOOT_MODE1
- TP23 pad 1: /Control/PMIC_ON_REQ -> PMIC_ON_REQ
- U1 pad A8: /Peripherals/GPIO3_IO00 -> unconnected-(U1-PadA8)
- U1 pad B8: /Peripherals/GPIO3_IO01 -> unconnected-(U1-PadB8)
- U1 pad C9: /Peripherals/GPIO3_IO03 -> /Peripherals/LED_1
- U1 pad D9: /Peripherals/GPIO3_IO02 -> /Peripherals/LED_0
- U1 pad E3: Net-(U1-PadE3) -> /Peripherals/GPIO4_IO22
- U1 pad E4: Net-(U1-PadE4) -> /Peripherals/GPIO4_IO21
- U1 pad F17: unconnected-(U1-PadF17) -> /Control/UART5_TX
- U1 pad G13: unconnected-(U1-PadG13) -> /Control/UART5_RX
- U1 pad G14: unconnected-(U1-PadG14) -> /Control/UART3_RTS
- U1 pad G16: unconnected-(U1-PadG16) -> /Control/UART4_RX
- U1 pad G17: unconnected-(U1-PadG17) -> /Control/UART4_TX
- U1 pad H14: unconnected-(U1-PadH14) -> /Control/UART2_RTS
- U1 pad H15: unconnected-(U1-PadH15) -> /Control/UART3_CTS
- U1 pad H16: unconnected-(U1-PadH16) -> /Control/UART3_RX
- U1 pad H17: unconnected-(U1-PadH17) -> /Control/UART3_TX
- U1 pad J15: unconnected-(U1-PadJ15) -> /Control/UART2_CTS
- U1 pad J16: unconnected-(U1-PadJ16) -> /Control/UART2_RX
- U1 pad J17: unconnected-(U1-PadJ17) -> /Control/UART2_TX
- U1 pad K13: USB1_ID -> /Peripherals/USB1_ID_R
- U1 pad R10: /Control/GPIO_DVFS -> GPIO_DVFS
- U1 pad T10: Net-(U1-PadT10) -> /Control/BOOT_MODE0
- U1 pad T9: /Control/PMIC_ON_REQ -> PMIC_ON_REQ
- U1 pad U10: Net-(U1-PadU10) -> /Control/BOOT_MODE1
- U11 pad 1: Net-(U11-Pad1) -> unconnected-(U11-Pad1)
- U11 pad 10: Net-(U11-Pad1) -> unconnected-(U11-Pad1)
- U11 pad 2: Net-(U11-Pad2) -> unconnected-(U11-Pad2)
- U11 pad 9: Net-(U11-Pad2) -> unconnected-(U11-Pad2)
- U18 pad 10: unconnected-(U18-Pad10) -> /Ethernet/RJ45_TD_N
- U18 pad 11: unconnected-(U18-Pad11) -> /Ethernet/RJ45_TD_P
- U18 pad 2: unconnected-(U18-Pad2) -> /Ethernet/RJ45_LED_Y_R
- U18 pad 4: unconnected-(U18-Pad4) -> /Ethernet/RJ45_LED_G_R
- U18 pad 7: unconnected-(U18-Pad7) -> /Ethernet/RJ45_RD_N
- U18 pad 8: unconnected-(U18-Pad8) -> /Ethernet/RJ45_RD_P
- U2 pad 1: unconnected-(U2-Pad1) -> /Power/PG_3V3
- U2 pad 2: unconnected-(U2-Pad2) -> GND
- U2 pad 3: unconnected-(U2-Pad3) -> Net-(U2-Pad3)
- U2 pad 4: unconnected-(U2-Pad4) -> VSYS_5V
- U2 pad 5: unconnected-(U2-Pad5) -> /Power/ARM_SOC_PG
- U2 pad 6: unconnected-(U2-Pad6) -> Net-(U2-Pad6)
- U20 pad 1: unconnected-(U20-Pad1) -> /Power/PG_3V3
- U20 pad 2: unconnected-(U20-Pad2) -> GND
- U20 pad 3: unconnected-(U20-Pad3) -> Net-(U20-Pad3)
- U20 pad 4: unconnected-(U20-Pad4) -> VSYS_5V
- U20 pad 5: unconnected-(U20-Pad5) -> /Power/DDR_PG
- U20 pad 6: unconnected-(U20-Pad6) -> Net-(U20-Pad6)
- U22 pad 1: LDO_3V3 -> /Power/LDO_3V3_R
- U23 pad 1: Net-(C17-Pad1) -> /Power/LDO_1V8_R
- U24 pad 4: unconnected-(U24-Pad4) -> Net-(U24-Pad4)
- U24 pad 5: Net-(C18-Pad1) -> /Power/SD_3V3_1V8_R
- U25 pad 1: Net-(U25-Pad1) -> /Ethernet/RJ45_TD_P
- U25 pad 10: Net-(U25-Pad1) -> /Ethernet/RJ45_TD_P
- U25 pad 2: Net-(U25-Pad2) -> /Ethernet/RJ45_TD_N
- U25 pad 3: Net-(U25-Pad3) -> GND
- U25 pad 4: Net-(U25-Pad4) -> /Ethernet/RJ45_RD_P
- U25 pad 5: Net-(U25-Pad5) -> /Ethernet/RJ45_RD_N
- U25 pad 6: Net-(U25-Pad5) -> /Ethernet/RJ45_RD_N
- U25 pad 7: Net-(U25-Pad4) -> /Ethernet/RJ45_RD_P
- U25 pad 8: Net-(U25-Pad3) -> GND
- U25 pad 9: Net-(U25-Pad2) -> /Ethernet/RJ45_TD_N
- U6 pad 1: unconnected-(U6-Pad1) -> /USB/CC2
- U6 pad 10: unconnected-(U6-Pad1) -> /USB/CC2
- U6 pad 4: /USB/USBD_P -> /USB/USB1D_P
- U6 pad 5: /USB/USBD_N -> /USB/USB1D_N
- U6 pad 6: /USB/USBD_N -> /USB/USB1D_N
- U6 pad 7: /USB/USBD_P -> /USB/USB1D_P
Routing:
- net /Ethernet/RJ45_TD_P: track 0.00 -> 12.2 mm
- net GND: track 134.2 -> 145.7 mm, vias 51 -> 63
- net /Ethernet/RJ45_TD_N: track 0.00 -> 10.7 mm, vias 0 -> 1
- net /Ethernet/RJ45_RD_P: track 0.00 -> 9.16 mm, vias 0 -> 2
- net /Ethernet/RJ45_RD_N: track 0.00 -> 9.05 mm, vias 0 -> 1
- net /USB/USB1D_P: track 0.00 -> 8.04 mm
- net /USB/USB1D_N: track 0.00 -> 8.00 mm
- net /USB/USB2D_P: track 0.00 -> 7.71 mm
- net /USB/USB2D_N: track 0.00 -> 7.71 mm
- net /USB/CC2: track 0.00 -> 6.42 mm
- net Net-(R40-Pad1): track 0.00 -> 6.23 mm
- net /USB/CC1: track 0.00 -> 4.87 mm, vias 0 -> 2
- net USB1_ID: track 0.00 -> 4.45 mm
- net Net-(R115-Pad2): track 0.00 -> 1.44 mm
- net DDR_1V35: track 44.6 -> 45.9 mm
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- added copper zone on F.Cu, net /USB/VBUS_1
- added copper zone on F.Cu, net VSYS_5V
